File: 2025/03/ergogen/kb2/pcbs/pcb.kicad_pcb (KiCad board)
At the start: 2 copper layers, 235 x 72 mm, 61 parts

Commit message: change pins for keys
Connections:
- D1 pad 1: GP10 -> GP9
- D10 pad 1: GP6 -> GP5
- D11 pad 1: GP10 -> GP22
- D12 pad 1: GP6 -> GP28
- D13 pad 1: GP10 -> GP22
- D14 pad 1: GP6 -> GP28
- D15 pad 1: GP10 -> GP22
- D16 pad 1: GP6 -> GP28
- D17 pad 1: GP10 -> GP22
- D18 pad 1: GP6 -> GP28
- D19 pad 1: GP10 -> GP22
- D2 pad 1: GP6 -> GP5
- D20 pad 1: GP6 -> GP28
- D21 pad 1: GP10 -> GP22
- D22 pad 1: GP6 -> GP28
- D3 pad 1: GP10 -> GP9
- D4 pad 1: GP6 -> GP5
- D5 pad 1: GP10 -> GP9
- D6 pad 1: GP6 -> GP5
- D7 pad 1: GP10 -> GP9
- D8 pad 1: GP6 -> GP5
- D9 pad 1: GP10 -> GP9
- S1 pad 1: GP1 -> GP10
- S10 pad 1: GP5 -> GP14
- S11 pad 1: GP5 -> GP16
- S12 pad 1: GP5 -> GP16
- S13 pad 1: GP4 -> GP17
- S14 pad 1: GP4 -> GP17
- S15 pad 1: GP3 -> GP18
- S16 pad 1: GP3 -> GP18
- S17 pad 1: GP2 -> GP19
- S18 pad 1: GP2 -> GP19
- S19 pad 1: GP1 -> GP20
- S2 pad 1: GP1 -> GP10
- S20 pad 1: GP1 -> GP20
- S21 pad 1: GP0 -> GP21
- S22 pad 1: GP0 -> GP21
- S23 pad 1: GP4 -> GP13
- S24 pad 1: GP5 -> GP14
- S25 pad 1: GP5 -> GP16
- S26 pad 1: GP4 -> GP17
- S3 pad 1: GP2 -> GP11
- S4 pad 1: GP2 -> GP11
- S5 pad 1: GP3 -> GP12
- S6 pad 1: GP3 -> GP12
- S7 pad 1: GP4 -> GP13
- S8 pad 1: GP4 -> GP13
- S9 pad 1: GP5 -> GP14
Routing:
- net GP10: track 0.00 -> 174.0 mm
- net GP11: track 0.00 -> 157.1 mm
- net GP12: track 0.00 -> 138.0 mm
- net GP13: track 0.00 -> 124.1 mm
- net GND: track 0.00 -> 120.2 mm
- net GP15: track 0.00 -> 110.6 mm
- net GP14: track 0.00 -> 104.7 mm
- net RUN: track 0.00 -> 40.2 mm
- net GP17: track 0.00 -> 34.0 mm
- net GP16: track 0.00 -> 15.3 mm

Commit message: finish wiring
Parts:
- moved _6 9.00 mm to (154.0, 117.0)
- moved _7 9.00 mm to (241.0, 117.0)
- turned B1 to 180 degrees
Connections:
- S1 pad 1: GP10 -> GP14
- S10 pad 1: GP14 -> GP10
- S11 pad 1: GP16 -> GP21
- S12 pad 1: GP16 -> GP21
- S13 pad 1: GP17 -> GP20
- S14 pad 1: GP17 -> GP20
- S15 pad 1: GP18 -> GP19
- S16 pad 1: GP18 -> GP19
- S17 pad 1: GP19 -> GP18
- S18 pad 1: GP19 -> GP18
- S19 pad 1: GP20 -> GP17
- S2 pad 1: GP10 -> GP14
- S20 pad 1: GP20 -> GP17
- S21 pad 1: GP21 -> GP16
- S22 pad 1: GP21 -> GP16
- S23 pad 1: GP13 -> GP11
- S24 pad 1: GP14 -> GP10
- S25 pad 1: GP16 -> GP21
- S26 pad 1: GP17 -> GP20
- S3 pad 1: GP11 -> GP13
- S4 pad 1: GP11 -> GP13
- S7 pad 1: GP13 -> GP11
- S8 pad 1: GP13 -> GP11
- S9 pad 1: GP14 -> GP10
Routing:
- net GP16: track 15.3 -> 185.3 mm
- net GP18: track 0.00 -> 151.6 mm
- net GP17: track 34.0 -> 170.0 mm
- net GP28: track 0.00 -> 135.6 mm
- net GP19: track 0.00 -> 135.5 mm
- net GP22: track 0.00 -> 134.5 mm
- net GP20: track 0.00 -> 127.2 mm
- net GP9: track 0.00 -> 119.8 mm
- net GP5: track 0.00 -> 119.7 mm
- net GP14: track 104.7 -> 182.2 mm
- net GP21: track 0.00 -> 66.6 mm
- net inner_top: track 0.00 -> 59.7 mm
- net GP10: track 174.0 -> 124.6 mm
- net outer_top: track 0.00 -> 44.8 mm
- net GP13: track 124.1 -> 168.0 mm
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
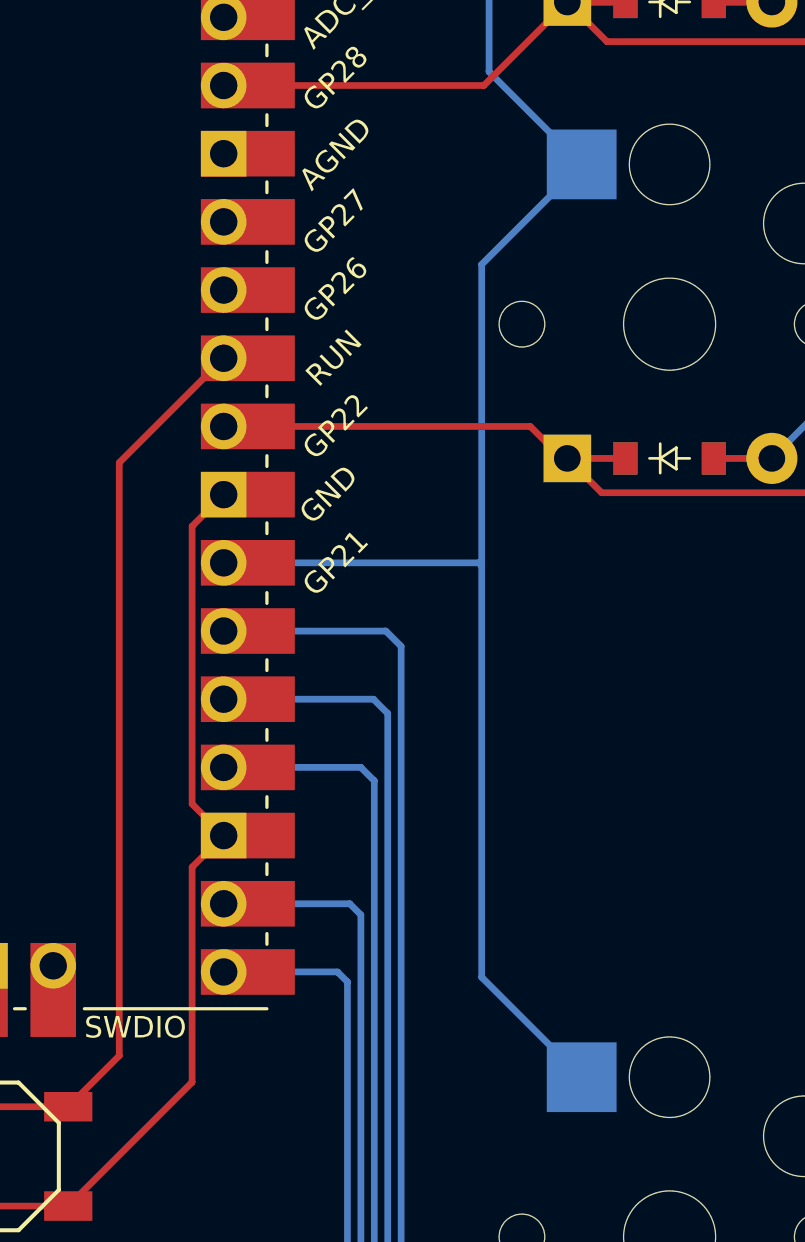
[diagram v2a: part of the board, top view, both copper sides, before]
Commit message: small pcb tweaks, generate gerber
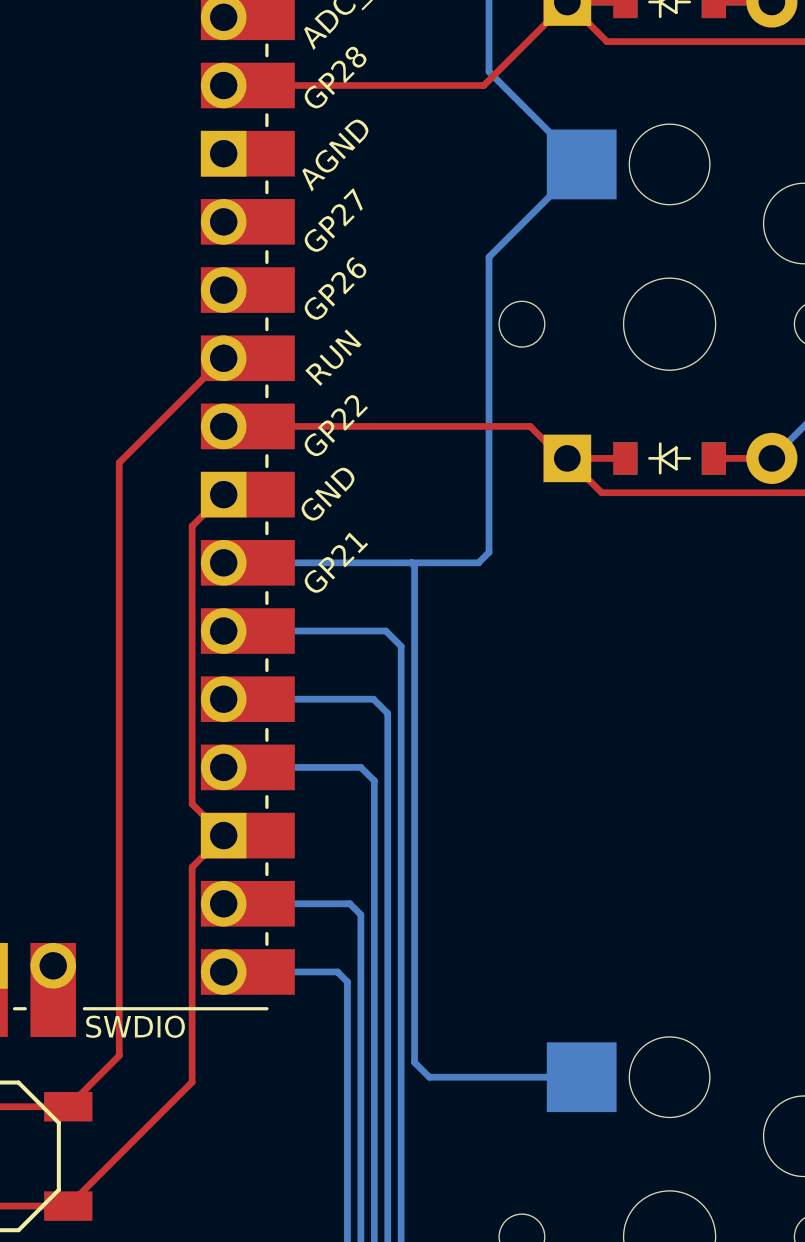
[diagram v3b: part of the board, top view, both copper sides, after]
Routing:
- net GP21: track 66.6 -> 70.9 mm
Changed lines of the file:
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@@
 		(0 "F.Cu" signal)
 		(2 "B.Cu" signal)
-		(9 "F.Adhes" user)
-		(11 "B.Adhes" user)
+		(9 "F.Adhes" user "F.Adhesive")
+		(11 "B.Adhes" user "B.Adhesive")
 		(13 "F.Paste" user)
 		(15 "B.Paste" user)
-		(5 "F.SilkS" user)
-		(7 "B.SilkS" user)
+		(5 "F.SilkS" user "F.Silkscreen")
+		(7 "B.SilkS" user "B.Silkscreen")
 		(1 "F.Mask" user)
 		(3 "B.Mask" user)
-		(17 "Dwgs.User" user)
-		(19 "Cmts.User" user)
-		(21 "Eco1.User" user)
-		(23 "Eco2.User" user)
+		(17 "Dwgs.User" user "User.Drawings")
+		(19 "Cmts.User" user "User.Comments")
+		(21 "Eco1.User" user "User.Eco1")
+		(23 "Eco2.User" user "User.Eco2")
 		(25 "Edge.Cuts" user)
 		(27 "Margin" user)
-		(31 "F.CrtYd" user)
-		(29 "B.CrtYd" user)
+		(31 "F.CrtYd" user "F.Courtyard")
+		(29 "B.CrtYd" user "B.Courtyard")
 		(35 "F.Fab" user)
 		(33 "B.Fab" user)
@@
 			(outputformat 1)
 			(mirror no)
-			(drillshape 1)
+			(drillshape 0)
 			(scaleselection 1)
-			(outputdirectory "")
+			(outputdirectory "../gerbers/")
 		)
 	)
@@
 	)
 	(segment
-		(start 216 109)
-		(end 216 97.775)
+		(start 214.05 128.05)
+		(end 219.725 128.05)
+		(width 0.25)
+		(layer "B.Cu")
+		(net 16)
+	)
+	(segment
+		(start 213.5 109)
+		(end 213.5 127.5)
 		(width 0.25)
 		(layer "B.Cu")
@@
 	)
 	(segment
-		(start 215.89 108.89)
-		(end 216 109)
+		(start 213.39 108.89)
+		(end 215.8831 108.89)
 		(width 0.25)
 		(layer "B.Cu")
@@
 	)
 	(segment
-		(start 216.2731 80.5019)
-		(end 219.725 77.05)
+		(start 215.8831 108.89)
+		(end 216.2731 108.5)
 		(width 0.25)
 		(layer "B.Cu")
@@
 	)
 	(segment
-		(start 216.2731 90.5981)
-		(end 216.2731 80.5019)
+		(start 213.5 127.5)
+		(end 214.05 128.05)
 		(width 0.25)
 		(layer "B.Cu")
@@
 	)
 	(segment
-		(start 206.39 108.89)
-		(end 215.89 108.89)
+		(start 216.2731 97.5019)
+		(end 219.725 94.05)
 		(width 0.25)
 		(layer "B.Cu")
@@
 	)
 	(segment
-		(start 216 97.775)
-		(end 219.725 94.05)
+		(start 213.39 108.89)
+		(end 213.5 109)
 		(width 0.25)
 		(layer "B.Cu")
@@
 	)
 	(segment
-		(start 216 124.325)
-		(end 216 109)
+		(start 216.2731 80.5019)
+		(end 219.725 77.05)
+		(width 0.25)
+		(layer "B.Cu")
+		(net 16)
+	)
+	(segment
+		(start 216.2731 90.5981)
+		(end 216.2731 80.5019)
+		(width 0.25)
+		(layer "B.Cu")
+		(net 16)
+	)
+	(segment
+		(start 206.39 108.89)
+		(end 213.39 108.89)
 		(width 0.25)
 		(layer "B.Cu")
@@
 	)
 	(segment
-		(start 219.725 128.05)
-		(end 216 124.325)
+		(start 216.2731 108.5)
+		(end 216.2731 97.5019)
 		(width 0.25)
 		(layer "B.Cu")
